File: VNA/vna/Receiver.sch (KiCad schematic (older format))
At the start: 13 parts

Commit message: power and rf src blocks added
battery managemet and rf source heirachical schematics have been added.

these schematics are still empty however will server as a test for visual diff.
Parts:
- U?: symbol dk_RF-Detectors:AD8302ARUZ -> vna-rescue:AD8302ARUZ-dk_RF-Detectors
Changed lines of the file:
@@
 $Descr A4 11693 8268
 encoding utf-8
-Sheet 7 8
+Sheet 7 9
 Title ""
 Date ""
@@
 $EndDescr
 $Comp
-L dk_RF-Detectors:AD8302ARUZ U?
+L vna-rescue:AD8302ARUZ-dk_RF-Detectors U?
 U 1 1 5CCBAC6E
 P 5450 3150

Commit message: adjusted main schematic to suit initial presentation
i moved a few blocks around so that the cropped version of the block diagram would fit nicely in my semester 1 presentation
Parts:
- gave numbers to parts that had none: 13
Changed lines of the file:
@@
 P 5450 3150
 AR Path="/5CCBAC6E" Ref="U?"  Part="1"
-AR Path="/5CCB994F/5CCBAC6E" Ref="U?"  Part="1"
-F 0 "U?" H 4900 2600 60  0000 C CNN
+AR Path="/5CCB994F/5CCBAC6E" Ref="U1"  Part="1"
+F 0 "U1" H 4900 2600 60  0000 C CNN
 F 1 "AD8302ARUZ" H 4750 2750 60  0000 C CNN
 F 2 "digikey-footprints:TSSOP-14_W4.4mm" H 5650 3350 60  0001 L CNN
@@
 	5950 3250 5950 3300
 $Comp
-L Device:C_Small C?
+L Device:C_Small C9
 U 1 1 5CCBBCEF
 P 6050 2750
-F 0 "C?" H 6142 2796 50  0000 L CNN
+F 0 "C9" H 6142 2796 50  0000 L CNN
 F 1 "DNP" H 6142 2705 50  0000 L CNN
 F 2 "" H 6050 2750 50  0001 C CNN
@@
 $EndComp
 $Comp
-L Device:C_Small C?
+L Device:C_Small C11
 U 1 1 5CCBCC6F
 P 6050 3550
-F 0 "C?" H 6142 3596 50  0000 L CNN
+F 0 "C11" H 6142 3596 50  0000 L CNN
 F 1 "DNP" H 6142 3505 50  0000 L CNN
 F 2 "" H 6050 3550 50  0001 C CNN
@@
 $EndComp
 $Comp
-L Device:C_Small C?
+L Device:C_Small C7
 U 1 1 5CCBEACE
 P 4950 2600
-F 0 "C?" H 4950 2550 50  0000 R CNN
+F 0 "C7" H 4950 2550 50  0000 R CNN
 F 1 "1n" H 4950 2700 50  0000 R CNN
 F 2 "" H 4950 2600 50  0001 C CNN
@@
 	5950 3450 6050 3450
 $Comp
-L Device:C_Small C?
+L Device:C_Small C10
 U 1 1 5CCC193D
 P 4750 3050
-F 0 "C?" V 4800 2900 50  0000 C CNN
+F 0 "C10" V 4800 2900 50  0000 C CNN
 F 1 "1n" V 4700 2950 50  0000 C CNN
 F 2 "" H 4750 3050 50  0001 C CNN
@@
 $EndComp
 $Comp
-L power:GNDD #PWR?
+L power:GNDD #PWR020
 U 1 1 5CCC1AA3
 P 5500 3700
-F 0 "#PWR?" H 5500 3450 50  0001 C CNN
+F 0 "#PWR020" H 5500 3450 50  0001 C CNN
 F 1 "GNDD" H 5504 3545 50  0000 C CNN
 F 2 "" H 5500 3700 50  0001 C CNN
@@
 	4950 2500 4950 2300
 $Comp
-L power:VDD #PWR?
+L power:VDD #PWR016
 U 1 1 5CCC3643
 P 5450 2450
-F 0 "#PWR?" H 5450 2300 50  0001 C CNN
+F 0 "#PWR016" H 5450 2300 50  0001 C CNN
 F 1 "VDD" H 5467 2623 50  0000 C CNN
 F 2 "" H 5450 2450 50  0001 C CNN
@@
 	5450 2450 5450 2550
 $Comp
-L Device:C_Small C?
+L Device:C_Small C5
 U 1 1 5CCC467E
 P 5600 2550
-F 0 "C?" V 5371 2550 50  0000 C CNN
+F 0 "C5" V 5371 2550 50  0000 C CNN
 F 1 "1n" V 5462 2550 50  0000 C CNN
 F 2 "" H 5600 2550 50  0001 C CNN
@@
 	5450 2550 5450 2650
 $Comp
-L power:GNDD #PWR?
+L power:GNDD #PWR018
 U 1 1 5CCC4AF9
 P 5800 2550
-F 0 "#PWR?" H 5800 2300 50  0001 C CNN
+F 0 "#PWR018" H 5800 2300 50  0001 C CNN
 F 1 "GNDD" H 5804 2395 50  0000 C CNN
 F 2 "" H 5800 2550 50  0001 C CNN
@@
 	5700 2550 5800 2550
 $Comp
-L power:GNDD #PWR?
+L power:GNDD #PWR019
 U 1 1 5CCC549F
 P 6400 2650
-F 0 "#PWR?" H 6400 2400 50  0001 C CNN
+F 0 "#PWR019" H 6400 2400 50  0001 C CNN
 F 1 "GNDD" H 6500 2650 50  0000 C CNN
 F 2 "" H 6400 2650 50  0001 C CNN
@@
 	6050 2650 6400 2650
 $Comp
-L power:GNDD #PWR?
+L power:GNDD #PWR021
 U 1 1 5CCC6234
 P 6050 3750
-F 0 "#PWR?" H 6050 3500 50  0001 C CNN
+F 0 "#PWR021" H 6050 3500 50  0001 C CNN
 F 1 "GNDD" H 6054 3595 50  0000 C CNN
 F 2 "" H 6050 3750 50  0001 C CNN
@@
 	5950 3150 6150 3150
 $Comp
-L Device:R_Small_US R?
+L Device:R_Small_US R8
 U 1 1 5CCC8149
 P 6350 3300
-F 0 "R?" V 6300 3400 50  0000 C CNN
+F 0 "R8" V 6300 3400 50  0000 C CNN
 F 1 "47" V 6400 3400 50  0000 C CNN
 F 2 "" H 6350 3300 50  0001 C CNN
@@
 	6450 3300 6750 3300
 $Comp
-L Device:R_Small_US R?
+L Device:R_Small_US R7
 U 1 1 5CCCB417
 P 6350 3000
-F 0 "R?" V 6300 3100 50  0000 C CNN
+F 0 "R7" V 6300 3100 50  0000 C CNN
 F 1 "47" V 6400 3100 50  0000 C CNN
 F 2 "" H 6350 3000 50  0001 C CNN
@@
 	4650 3050 4400 3050
 $Comp
-L Device:C_Small C?
+L Device:C_Small C6
 U 1 1 5CCCD139
 P 4400 2600
-F 0 "C?" H 4308 2554 50  0000 R CNN
+F 0 "C6" H 4308 2554 50  0000 R CNN
 F 1 "1n" H 4308 2645 50  0000 R CNN
 F 2 "" H 4400 2600 50  0001 C CNN
@@
 	4400 2700 4400 3050
 $Comp
-L Device:R_Small_US R?
+L Device:R_Small_US R5
 U 1 1 5CCCE370
 P 4500 2300
-F 0 "R?" V 4400 2250 50  0000 C CNN
+F 0 "R5" V 4400 2250 50  0000 C CNN
 F 1 "50" V 4600 2300 50  0000 C CNN
 F 2 "" H 4500 2300 50  0001 C CNN
@@
 	4400 2300 4400 2500
 $Comp
-L Device:R_Small_US R?
+L Device:R_Small_US R6
 U 1 1 5CCCE9E8
 P 4850 2300
-F 0 "R?" V 4750 2250 50  0000 C CNN
+F 0 "R6" V 4750 2250 50  0000 C CNN
 F 1 "50" V 4950 2300 50  0000 C CNN
 F 2 "" H 4850 2300 50  0001 C CNN
@@
 	4950 2300 4950 2100
 $Comp
-L power:GNDD #PWR?
+L power:GNDD #PWR015
 U 1 1 5CCCF1A1
 P 4650 2300
-F 0 "#PWR?" H 4650 2050 50  0001 C CNN
+F 0 "#PWR015" H 4650 2050 50  0001 C CNN
 F 1 "GNDD" H 4650 2150 50  0000 C CNN
 F 2 "" H 4650 2300 50  0001 C CNN
@@
 	3550 2850 3550 3150
 $Comp
-L Device:C_Small C?
+L Device:C_Small C8
 U 1 1 5CCD1372
 P 3550 2750
-F 0 "C?" H 3642 2796 50  0000 L CNN
+F 0 "C8" H 3642 2796 50  0000 L CNN
 F 1 "C_Small" H 3642 2705 50  0000 L CNN
 F 2 "" H 3550 2750 50  0001 C CNN
@@
 $EndComp
 $Comp
-L Device:C_Small C?
+L Device:C_Small C4
 U 1 1 5CCD1C01
 P 3550 2400
-F 0 "C?" H 3642 2446 50  0000 L CNN
+F 0 "C4" H 3642 2446 50  0000 L CNN
 F 1 "C_Small" H 3642 2355 50  0000 L CNN
 F 2 "" H 3550 2400 50  0001 C CNN
@@
 OffsetA
 $Comp
-L power:GNDD #PWR?
+L power:GNDD #PWR017
 U 1 1 5CCD6524
 P 3300 2550
-F 0 "#PWR?" H 3300 2300 50  0001 C CNN
+F 0 "#PWR017" H 3300 2300 50  0001 C CNN
 F 1 "GNDD" H 3304 2395 50  0000 C CNN
 F 2 "" H 3300 2550 50  0001 C CNN

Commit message: micro-controller pins labelled
micro controller pins have been labelled, the pins on the bottom are yet to be linked to them.

still to wire up ftdi chip,

still to decide upon rf switch control schema.
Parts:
- C3: renamed from C4; value C_Small -> 1n
- C7: renamed from C8; value C_Small -> 1n
- renumbered C11 to C10, C5 to C4, C6 to C5, C7 to C6, C9 to C8, C10 to C9
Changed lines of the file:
@@
 $Descr A4 11693 8268
 encoding utf-8
-Sheet 7 10
+Sheet 6 10
 Title ""
 Date ""
@@
 	5950 3250 5950 3300
 $Comp
-L Device:C_Small C9
+L Device:C_Small C8
 U 1 1 5CCBBCEF
 P 6050 2750
-F 0 "C9" H 6142 2796 50  0000 L CNN
+F 0 "C8" H 6142 2796 50  0000 L CNN
 F 1 "DNP" H 6142 2705 50  0000 L CNN
 F 2 "" H 6050 2750 50  0001 C CNN
@@
 $EndComp
 $Comp
-L Device:C_Small C11
+L Device:C_Small C10
 U 1 1 5CCBCC6F
 P 6050 3550
-F 0 "C11" H 6142 3596 50  0000 L CNN
+F 0 "C10" H 6142 3596 50  0000 L CNN
 F 1 "DNP" H 6142 3505 50  0000 L CNN
 F 2 "" H 6050 3550 50  0001 C CNN
@@
 $EndComp
 $Comp
-L Device:C_Small C7
+L Device:C_Small C6
 U 1 1 5CCBEACE
 P 4950 2600
-F 0 "C7" H 4950 2550 50  0000 R CNN
+F 0 "C6" H 4950 2550 50  0000 R CNN
 F 1 "1n" H 4950 2700 50  0000 R CNN
 F 2 "" H 4950 2600 50  0001 C CNN
@@
 	5950 3450 6050 3450
 $Comp
-L Device:C_Small C10
+L Device:C_Small C9
 U 1 1 5CCC193D
 P 4750 3050
-F 0 "C10" V 4800 2900 50  0000 C CNN
+F 0 "C9" V 4800 2900 50  0000 C CNN
 F 1 "1n" V 4700 2950 50  0000 C CNN
 F 2 "" H 4750 3050 50  0001 C CNN
@@
 	5450 2450 5450 2550
 $Comp
-L Device:C_Small C5
+L Device:C_Small C4
 U 1 1 5CCC467E
 P 5600 2550
-F 0 "C5" V 5371 2550 50  0000 C CNN
+F 0 "C4" V 5371 2550 50  0000 C CNN
 F 1 "1n" V 5462 2550 50  0000 C CNN
 F 2 "" H 5600 2550 50  0001 C CNN
@@
 	4650 3050 4400 3050
 $Comp
-L Device:C_Small C6
+L Device:C_Small C5
 U 1 1 5CCCD139
 P 4400 2600
-F 0 "C6" H 4308 2554 50  0000 R CNN
+F 0 "C5" H 4308 2554 50  0000 R CNN
 F 1 "1n" H 4308 2645 50  0000 R CNN
 F 2 "" H 4400 2600 50  0001 C CNN
@@
 	3550 2850 3550 3150
 $Comp
-L Device:C_Small C8
+L Device:C_Small C7
 U 1 1 5CCD1372
 P 3550 2750
-F 0 "C8" H 3642 2796 50  0000 L CNN
-F 1 "C_Small" H 3642 2705 50  0000 L CNN
+F 0 "C7" H 3642 2796 50  0000 L CNN
+F 1 "1n" H 3642 2705 50  0000 L CNN
 F 2 "" H 3550 2750 50  0001 C CNN
 F 3 "~" H 3550 2750 50  0001 C CNN
@@
 $EndComp
 $Comp
-L Device:C_Small C4
+L Device:C_Small C3
 U 1 1 5CCD1C01
 P 3550 2400
-F 0 "C4" H 3642 2446 50  0000 L CNN
-F 1 "C_Small" H 3642 2355 50  0000 L CNN
+F 0 "C3" H 3642 2446 50  0000 L CNN
+F 1 "1n" H 3642 2355 50  0000 L CNN
 F 2 "" H 3550 2400 50  0001 C CNN
 F 3 "~" H 3550 2400 50  0001 C CNN

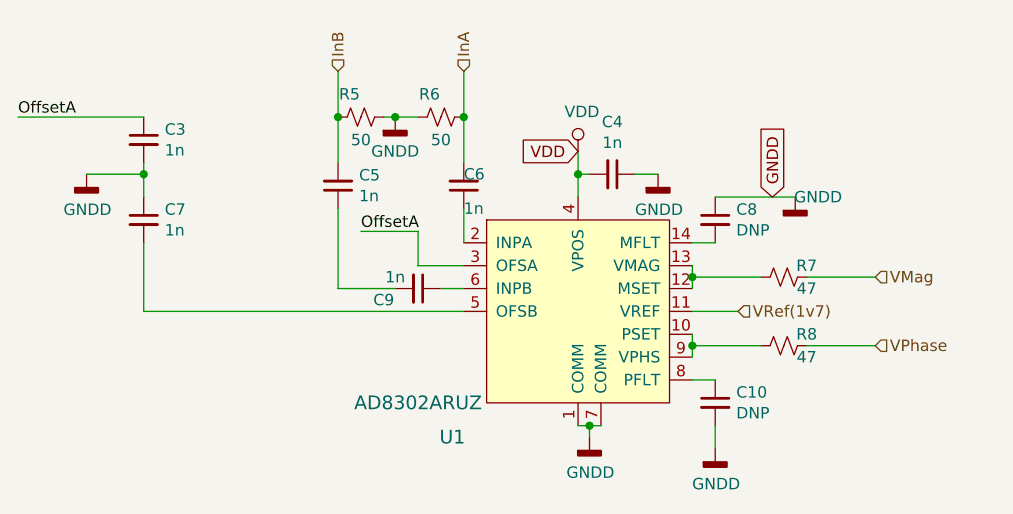
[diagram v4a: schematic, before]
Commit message: finished controller, chose compatible switches
controller and rf switches have been completed.

ToDo: finish filter design for RF Source, add auto gain control
ToDo: finish directional coupler footprints
ToDo: PCB Layout
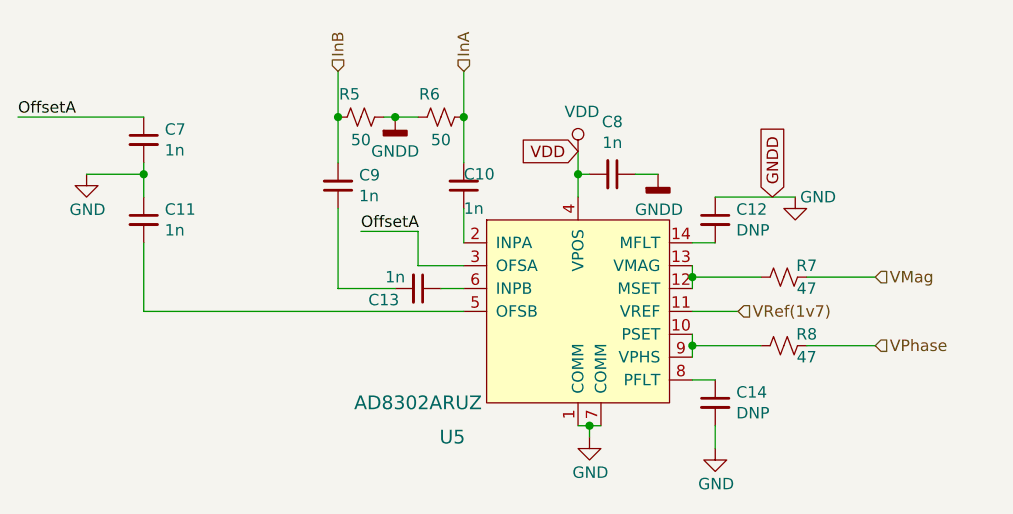
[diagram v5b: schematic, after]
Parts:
- C10: renamed from C6; footprint (none) -> Capacitor_SMD:C_0805_2012Metric_Pad1.15x1.40mm_HandSolder
- C11: renamed from C7; footprint (none) -> Capacitor_SMD:C_0805_2012Metric_Pad1.15x1.40mm_HandSolder
- C12: renamed from C8; footprint (none) -> Capacitor_SMD:C_0805_2012Metric_Pad1.15x1.40mm_HandSolder
- C13: renamed from C9; footprint (none) -> Capacitor_SMD:C_0805_2012Metric_Pad1.15x1.40mm_HandSolder
- C14: renamed from C10; footprint (none) -> Capacitor_SMD:C_0805_2012Metric_Pad1.15x1.40mm_HandSolder
- C7: renamed from C3; footprint (none) -> Capacitor_SMD:C_0805_2012Metric_Pad1.15x1.40mm_HandSolder
- C8: renamed from C4; footprint (none) -> Capacitor_SMD:C_0805_2012Metric_Pad1.15x1.40mm_HandSolder
- C9: renamed from C5; footprint (none) -> Capacitor_SMD:C_0805_2012Metric_Pad1.15x1.40mm_HandSolder
- R5, R6, R7, R8: footprint (none) -> Resistor_SMD:R_0805_2012Metric_Pad1.15x1.40mm_HandSolder
- renumbered U1 to U5
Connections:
- net GNDD renamed GND
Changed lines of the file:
@@
 P 5450 3150
 AR Path="/5CCBAC6E" Ref="U?"  Part="1"
-AR Path="/5CCB994F/5CCBAC6E" Ref="U1"  Part="1"
-F 0 "U1" H 4900 2600 60  0000 C CNN
+AR Path="/5CCB994F/5CCBAC6E" Ref="U5"  Part="1"
+F 0 "U5" H 4900 2600 60  0000 C CNN
 F 1 "AD8302ARUZ" H 4750 2750 60  0000 C CNN
 F 2 "digikey-footprints:TSSOP-14_W4.4mm" H 5650 3350 60  0001 L CNN
@@
 	5950 3250 5950 3300
 $Comp
-L Device:C_Small C8
+L Device:C_Small C12
 U 1 1 5CCBBCEF
 P 6050 2750
-F 0 "C8" H 6142 2796 50  0000 L CNN
+F 0 "C12" H 6142 2796 50  0000 L CNN
 F 1 "DNP" H 6142 2705 50  0000 L CNN
-F 2 "" H 6050 2750 50  0001 C CNN
+F 2 "Capacitor_SMD:C_0805_2012Metric_Pad1.15x1.40mm_HandSolder" H 6050 2750 50  0001 C CNN
 F 3 "~" H 6050 2750 50  0001 C CNN
 	1    6050 2750
@@
 $EndComp
 $Comp
-L Device:C_Small C10
+L Device:C_Small C14
 U 1 1 5CCBCC6F
 P 6050 3550
-F 0 "C10" H 6142 3596 50  0000 L CNN
+F 0 "C14" H 6142 3596 50  0000 L CNN
 F 1 "DNP" H 6142 3505 50  0000 L CNN
-F 2 "" H 6050 3550 50  0001 C CNN
+F 2 "Capacitor_SMD:C_0805_2012Metric_Pad1.15x1.40mm_HandSolder" H 6050 3550 50  0001 C CNN
 F 3 "~" H 6050 3550 50  0001 C CNN
 	1    6050 3550
@@
 $EndComp
 $Comp
-L Device:C_Small C6
+L Device:C_Small C10
 U 1 1 5CCBEACE
 P 4950 2600
-F 0 "C6" H 4950 2550 50  0000 R CNN
+F 0 "C10" H 4950 2550 50  0000 R CNN
 F 1 "1n" H 4950 2700 50  0000 R CNN
-F 2 "" H 4950 2600 50  0001 C CNN
+F 2 "Capacitor_SMD:C_0805_2012Metric_Pad1.15x1.40mm_HandSolder" H 4950 2600 50  0001 C CNN
 F 3 "~" H 4950 2600 50  0001 C CNN
 	1    4950 2600
@@
 	5950 3450 6050 3450
 $Comp
-L Device:C_Small C9
+L Device:C_Small C13
 U 1 1 5CCC193D
 P 4750 3050
-F 0 "C9" V 4800 2900 50  0000 C CNN
+F 0 "C13" V 4800 2900 50  0000 C CNN
 F 1 "1n" V 4700 2950 50  0000 C CNN
-F 2 "" H 4750 3050 50  0001 C CNN
+F 2 "Capacitor_SMD:C_0805_2012Metric_Pad1.15x1.40mm_HandSolder" H 4750 3050 50  0001 C CNN
 F 3 "~" H 4750 3050 50  0001 C CNN
 	1    4750 3050
@@
 $EndComp
 $Comp
-L power:GNDD #PWR020
+L power:GND #PWR023
 U 1 1 5CCC1AA3
 P 5500 3700
-F 0 "#PWR020" H 5500 3450 50  0001 C CNN
-F 1 "GNDD" H 5504 3545 50  0000 C CNN
+F 0 "#PWR023" H 5500 3450 50  0001 C CNN
+F 1 "GND" H 5504 3545 50  0000 C CNN
 F 2 "" H 5500 3700 50  0001 C CNN
 F 3 "" H 5500 3700 50  0001 C CNN
@@
 	4950 2500 4950 2300
 $Comp
-L power:VDD #PWR016
+L power:VDD #PWR019
 U 1 1 5CCC3643
 P 5450 2450
-F 0 "#PWR016" H 5450 2300 50  0001 C CNN
+F 0 "#PWR019" H 5450 2300 50  0001 C CNN
 F 1 "VDD" H 5467 2623 50  0000 C CNN
 F 2 "" H 5450 2450 50  0001 C CNN
@@
 	5450 2450 5450 2550
 $Comp
-L Device:C_Small C4
+L Device:C_Small C8
 U 1 1 5CCC467E
 P 5600 2550
-F 0 "C4" V 5371 2550 50  0000 C CNN
+F 0 "C8" V 5371 2550 50  0000 C CNN
 F 1 "1n" V 5462 2550 50  0000 C CNN
-F 2 "" H 5600 2550 50  0001 C CNN
+F 2 "Capacitor_SMD:C_0805_2012Metric_Pad1.15x1.40mm_HandSolder" H 5600 2550 50  0001 C CNN
 F 3 "~" H 5600 2550 50  0001 C CNN
 	1    5600 2550
@@
 	5450 2550 5450 2650
 $Comp
-L power:GNDD #PWR018
+L power:GNDD #PWR021
 U 1 1 5CCC4AF9
 P 5800 2550
-F 0 "#PWR018" H 5800 2300 50  0001 C CNN
+F 0 "#PWR021" H 5800 2300 50  0001 C CNN
 F 1 "GNDD" H 5804 2395 50  0000 C CNN
 F 2 "" H 5800 2550 50  0001 C CNN
@@
 	5700 2550 5800 2550
 $Comp
-L power:GNDD #PWR019
+L power:GND #PWR022
 U 1 1 5CCC549F
 P 6400 2650
-F 0 "#PWR019" H 6400 2400 50  0001 C CNN
-F 1 "GNDD" H 6500 2650 50  0000 C CNN
+F 0 "#PWR022" H 6400 2400 50  0001 C CNN
+F 1 "GND" H 6500 2650 50  0000 C CNN
 F 2 "" H 6400 2650 50  0001 C CNN
 F 3 "" H 6400 2650 50  0001 C CNN
@@
 	6050 2650 6400 2650
 $Comp
-L power:GNDD #PWR021
+L power:GND #PWR024
 U 1 1 5CCC6234
 P 6050 3750
-F 0 "#PWR021" H 6050 3500 50  0001 C CNN
-F 1 "GNDD" H 6054 3595 50  0000 C CNN
+F 0 "#PWR024" H 6050 3500 50  0001 C CNN
+F 1 "GND" H 6054 3595 50  0000 C CNN
 F 2 "" H 6050 3750 50  0001 C CNN
 F 3 "" H 6050 3750 50  0001 C CNN
@@
 F 0 "R8" V 6300 3400 50  0000 C CNN
 F 1 "47" V 6400 3400 50  0000 C CNN
-F 2 "" H 6350 3300 50  0001 C CNN
+F 2 "Resistor_SMD:R_0805_2012Metric_Pad1.15x1.40mm_HandSolder" H 6350 3300 50  0001 C CNN
 F 3 "~" H 6350 3300 50  0001 C CNN
 	1    6350 3300
@@
 F 0 "R7" V 6300 3100 50  0000 C CNN
 F 1 "47" V 6400 3100 50  0000 C CNN
-F 2 "" H 6350 3000 50  0001 C CNN
+F 2 "Resistor_SMD:R_0805_2012Metric_Pad1.15x1.40mm_HandSolder" H 6350 3000 50  0001 C CNN
 F 3 "~" H 6350 3000 50  0001 C CNN
 	1    6350 3000
@@
 	4650 3050 4400 3050
 $Comp
-L Device:C_Small C5
+L Device:C_Small C9
 U 1 1 5CCCD139
 P 4400 2600
-F 0 "C5" H 4308 2554 50  0000 R CNN
+F 0 "C9" H 4308 2554 50  0000 R CNN
 F 1 "1n" H 4308 2645 50  0000 R CNN
-F 2 "" H 4400 2600 50  0001 C CNN
+F 2 "Capacitor_SMD:C_0805_2012Metric_Pad1.15x1.40mm_HandSolder" H 4400 2600 50  0001 C CNN
 F 3 "~" H 4400 2600 50  0001 C CNN
 	1    4400 2600
@@
 F 0 "R5" V 4400 2250 50  0000 C CNN
 F 1 "50" V 4600 2300 50  0000 C CNN
-F 2 "" H 4500 2300 50  0001 C CNN
+F 2 "Resistor_SMD:R_0805_2012Metric_Pad1.15x1.40mm_HandSolder" H 4500 2300 50  0001 C CNN
 F 3 "~" H 4500 2300 50  0001 C CNN
 	1    4500 2300
@@
 F 0 "R6" V 4750 2250 50  0000 C CNN
 F 1 "50" V 4950 2300 50  0000 C CNN
-F 2 "" H 4850 2300 50  0001 C CNN
+F 2 "Resistor_SMD:R_0805_2012Metric_Pad1.15x1.40mm_HandSolder" H 4850 2300 50  0001 C CNN
 F 3 "~" H 4850 2300 50  0001 C CNN
 	1    4850 2300
@@
 	4950 2300 4950 2100
 $Comp
-L power:GNDD #PWR015
+L power:GNDD #PWR018
 U 1 1 5CCCF1A1
 P 4650 2300
-F 0 "#PWR015" H 4650 2050 50  0001 C CNN
+F 0 "#PWR018" H 4650 2050 50  0001 C CNN
 F 1 "GNDD" H 4650 2150 50  0000 C CNN
 F 2 "" H 4650 2300 50  0001 C CNN
@@
 	3550 2850 3550 3150
 $Comp
-L Device:C_Small C7
+L Device:C_Small C11
 U 1 1 5CCD1372
 P 3550 2750
-F 0 "C7" H 3642 2796 50  0000 L CNN
+F 0 "C11" H 3642 2796 50  0000 L CNN
 F 1 "1n" H 3642 2705 50  0000 L CNN
-F 2 "" H 3550 2750 50  0001 C CNN
+F 2 "Capacitor_SMD:C_0805_2012Metric_Pad1.15x1.40mm_HandSolder" H 3550 2750 50  0001 C CNN
 F 3 "~" H 3550 2750 50  0001 C CNN
 	1    3550 2750
@@
 $EndComp
 $Comp
-L Device:C_Small C3
+L Device:C_Small C7
 U 1 1 5CCD1C01
 P 3550 2400
-F 0 "C3" H 3642 2446 50  0000 L CNN
+F 0 "C7" H 3642 2446 50  0000 L CNN
 F 1 "1n" H 3642 2355 50  0000 L CNN
-F 2 "" H 3550 2400 50  0001 C CNN
+F 2 "Capacitor_SMD:C_0805_2012Metric_Pad1.15x1.40mm_HandSolder" H 3550 2400 50  0001 C CNN
 F 3 "~" H 3550 2400 50  0001 C CNN
 	1    3550 2400
@@
 OffsetA
 $Comp
-L power:GNDD #PWR017
+L power:GND #PWR020
 U 1 1 5CCD6524
 P 3300 2550
-F 0 "#PWR017" H 3300 2300 50  0001 C CNN
-F 1 "GNDD" H 3304 2395 50  0000 C CNN
+F 0 "#PWR020" H 3300 2300 50  0001 C CNN
+F 1 "GND" H 3304 2395 50  0000 C CNN
 F 2 "" H 3300 2550 50  0001 C CNN
 F 3 "" H 3300 2550 50  0001 C CNN

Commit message: custom footprint for couplers, added decoupling caps
added custom footprint for directional couplers - will need to verify it

added decoupling caps to ad9851
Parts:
- C10, C11, C12, C13, C14, C7, C8, C9: footprint Capacitor_SMD:C_0805_2012Metric_Pad1.15x1.40mm_HandSolder -> Capacitor_SMD:C_1206_3216Metric_Pad1.42x1.75mm_HandSolder
- R5, R6, R7, R8: footprint Resistor_SMD:R_0805_2012Metric_Pad1.15x1.40mm_HandSolder -> Resistor_SMD:R_1206_3216Metric_Pad1.42x1.75mm_HandSolder
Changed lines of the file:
@@
 F 0 "C12" H 6142 2796 50  0000 L CNN
 F 1 "DNP" H 6142 2705 50  0000 L CNN
-F 2 "Capacitor_SMD:C_0805_2012Metric_Pad1.15x1.40mm_HandSolder" H 6050 2750 50  0001 C CNN
+F 2 "Capacitor_SMD:C_1206_3216Metric_Pad1.42x1.75mm_HandSolder" H 6050 2750 50  0001 C CNN
 F 3 "~" H 6050 2750 50  0001 C CNN
 	1    6050 2750
@@
 F 0 "C14" H 6142 3596 50  0000 L CNN
 F 1 "DNP" H 6142 3505 50  0000 L CNN
-F 2 "Capacitor_SMD:C_0805_2012Metric_Pad1.15x1.40mm_HandSolder" H 6050 3550 50  0001 C CNN
+F 2 "Capacitor_SMD:C_1206_3216Metric_Pad1.42x1.75mm_HandSolder" H 6050 3550 50  0001 C CNN
 F 3 "~" H 6050 3550 50  0001 C CNN
 	1    6050 3550
@@
 F 0 "C10" H 4950 2550 50  0000 R CNN
 F 1 "1n" H 4950 2700 50  0000 R CNN
-F 2 "Capacitor_SMD:C_0805_2012Metric_Pad1.15x1.40mm_HandSolder" H 4950 2600 50  0001 C CNN
+F 2 "Capacitor_SMD:C_1206_3216Metric_Pad1.42x1.75mm_HandSolder" H 4950 2600 50  0001 C CNN
 F 3 "~" H 4950 2600 50  0001 C CNN
 	1    4950 2600
@@
 F 0 "C13" V 4800 2900 50  0000 C CNN
 F 1 "1n" V 4700 2950 50  0000 C CNN
-F 2 "Capacitor_SMD:C_0805_2012Metric_Pad1.15x1.40mm_HandSolder" H 4750 3050 50  0001 C CNN
+F 2 "Capacitor_SMD:C_1206_3216Metric_Pad1.42x1.75mm_HandSolder" H 4750 3050 50  0001 C CNN
 F 3 "~" H 4750 3050 50  0001 C CNN
 	1    4750 3050
@@
 F 0 "C8" V 5371 2550 50  0000 C CNN
 F 1 "1n" V 5462 2550 50  0000 C CNN
-F 2 "Capacitor_SMD:C_0805_2012Metric_Pad1.15x1.40mm_HandSolder" H 5600 2550 50  0001 C CNN
+F 2 "Capacitor_SMD:C_1206_3216Metric_Pad1.42x1.75mm_HandSolder" H 5600 2550 50  0001 C CNN
 F 3 "~" H 5600 2550 50  0001 C CNN
 	1    5600 2550
@@
 F 0 "R8" V 6300 3400 50  0000 C CNN
 F 1 "47" V 6400 3400 50  0000 C CNN
-F 2 "Resistor_SMD:R_0805_2012Metric_Pad1.15x1.40mm_HandSolder" H 6350 3300 50  0001 C CNN
+F 2 "Resistor_SMD:R_1206_3216Metric_Pad1.42x1.75mm_HandSolder" H 6350 3300 50  0001 C CNN
 F 3 "~" H 6350 3300 50  0001 C CNN
 	1    6350 3300
@@
 F 0 "R7" V 6300 3100 50  0000 C CNN
 F 1 "47" V 6400 3100 50  0000 C CNN
-F 2 "Resistor_SMD:R_0805_2012Metric_Pad1.15x1.40mm_HandSolder" H 6350 3000 50  0001 C CNN
+F 2 "Resistor_SMD:R_1206_3216Metric_Pad1.42x1.75mm_HandSolder" H 6350 3000 50  0001 C CNN
 F 3 "~" H 6350 3000 50  0001 C CNN
 	1    6350 3000
@@
 F 0 "C9" H 4308 2554 50  0000 R CNN
 F 1 "1n" H 4308 2645 50  0000 R CNN
-F 2 "Capacitor_SMD:C_0805_2012Metric_Pad1.15x1.40mm_HandSolder" H 4400 2600 50  0001 C CNN
+F 2 "Capacitor_SMD:C_1206_3216Metric_Pad1.42x1.75mm_HandSolder" H 4400 2600 50  0001 C CNN
 F 3 "~" H 4400 2600 50  0001 C CNN
 	1    4400 2600
@@
 F 0 "R5" V 4400 2250 50  0000 C CNN
 F 1 "50" V 4600 2300 50  0000 C CNN
-F 2 "Resistor_SMD:R_0805_2012Metric_Pad1.15x1.40mm_HandSolder" H 4500 2300 50  0001 C CNN
+F 2 "Resistor_SMD:R_1206_3216Metric_Pad1.42x1.75mm_HandSolder" H 4500 2300 50  0001 C CNN
 F 3 "~" H 4500 2300 50  0001 C CNN
 	1    4500 2300
@@
 F 0 "R6" V 4750 2250 50  0000 C CNN
 F 1 "50" V 4950 2300 50  0000 C CNN
-F 2 "Resistor_SMD:R_0805_2012Metric_Pad1.15x1.40mm_HandSolder" H 4850 2300 50  0001 C CNN
+F 2 "Resistor_SMD:R_1206_3216Metric_Pad1.42x1.75mm_HandSolder" H 4850 2300 50  0001 C CNN
 F 3 "~" H 4850 2300 50  0001 C CNN
 	1    4850 2300
@@
 F 0 "C11" H 3642 2796 50  0000 L CNN
 F 1 "1n" H 3642 2705 50  0000 L CNN
-F 2 "Capacitor_SMD:C_0805_2012Metric_Pad1.15x1.40mm_HandSolder" H 3550 2750 50  0001 C CNN
+F 2 "Capacitor_SMD:C_1206_3216Metric_Pad1.42x1.75mm_HandSolder" H 3550 2750 50  0001 C CNN
 F 3 "~" H 3550 2750 50  0001 C CNN
 	1    3550 2750
@@
 F 0 "C7" H 3642 2446 50  0000 L CNN
 F 1 "1n" H 3642 2355 50  0000 L CNN
-F 2 "Capacitor_SMD:C_0805_2012Metric_Pad1.15x1.40mm_HandSolder" H 3550 2400 50  0001 C CNN
+F 2 "Capacitor_SMD:C_1206_3216Metric_Pad1.42x1.75mm_HandSolder" H 3550 2400 50  0001 C CNN
 F 3 "~" H 3550 2400 50  0001 C CNN
 	1    3550 2400
